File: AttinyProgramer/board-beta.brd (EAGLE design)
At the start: 49 x 27.4 mm, 7 parts, among them IC1 ATTINY44-SSU

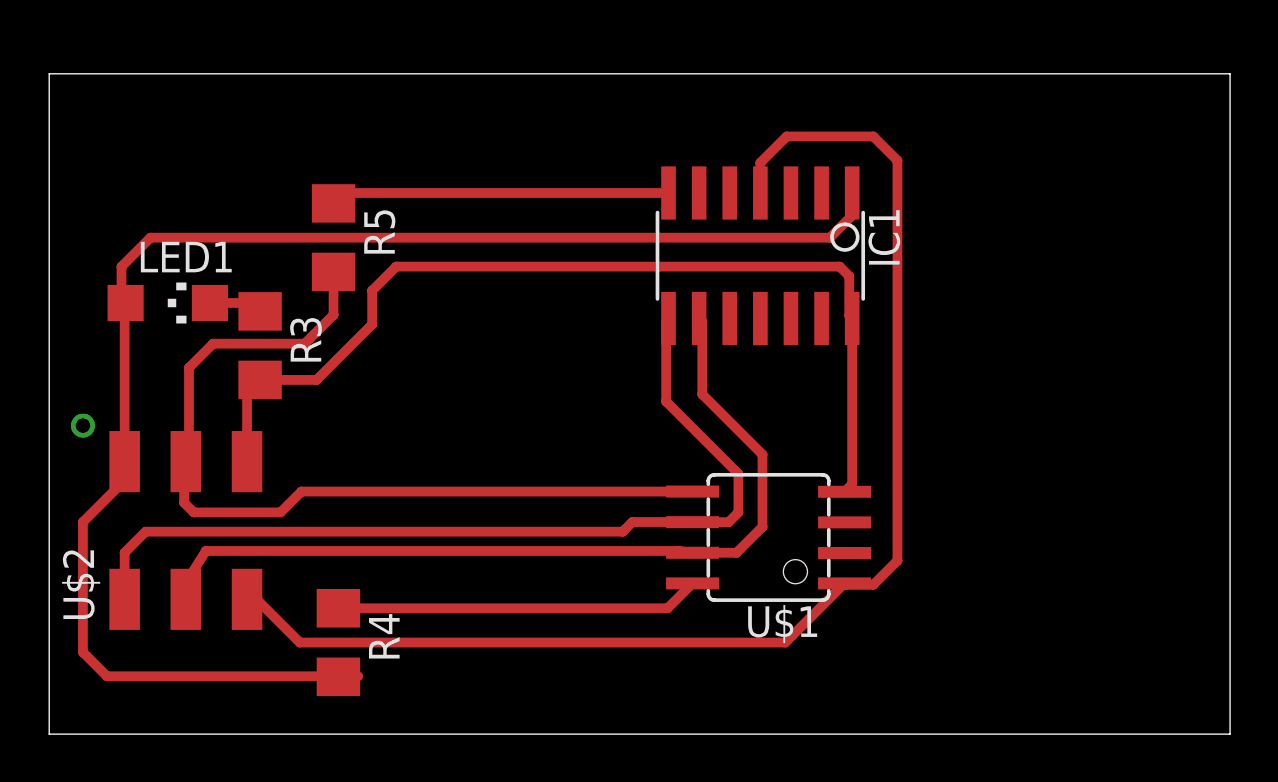
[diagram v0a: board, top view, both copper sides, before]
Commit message: add board programer bootloader
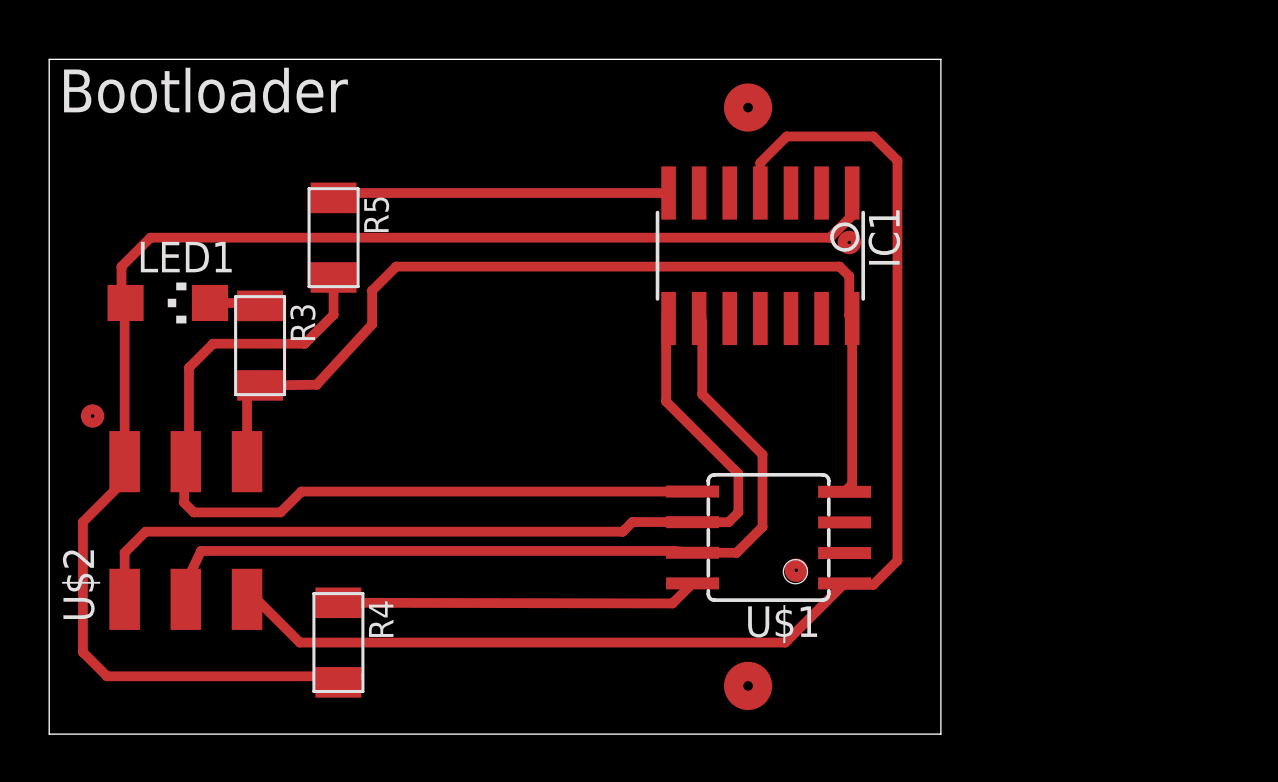
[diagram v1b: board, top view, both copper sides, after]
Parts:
- R3, R4, R5: device fab:R1206 -> fab:R1206FAB
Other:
- board size 49 x 27.4 mm -> 37 x 28 mm
- board text added: "Bootloader"
